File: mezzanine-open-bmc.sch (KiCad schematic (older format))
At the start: 2 parts, among them P1 CONN_02X20, P2 CONN_02X20

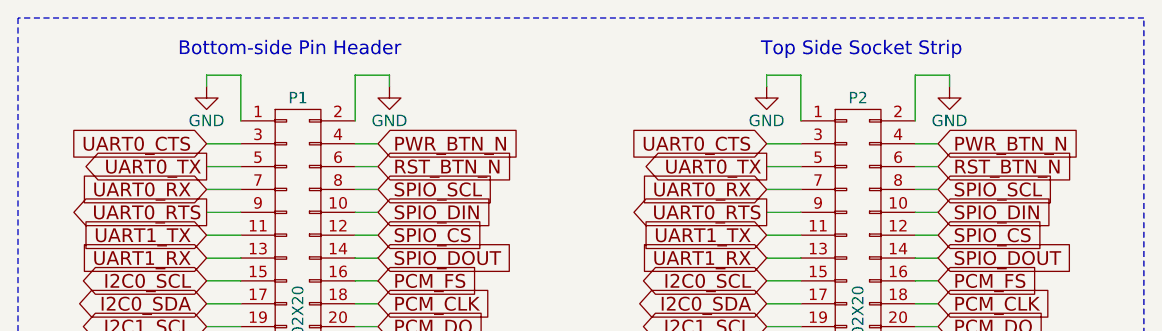
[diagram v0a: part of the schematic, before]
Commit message: Reset Project
The previous commits were based on an outdated template.
The project has been restarted with the up to date template.

Signed-off-by: Sophie Haynes <sophie.haynes@linaro.org>
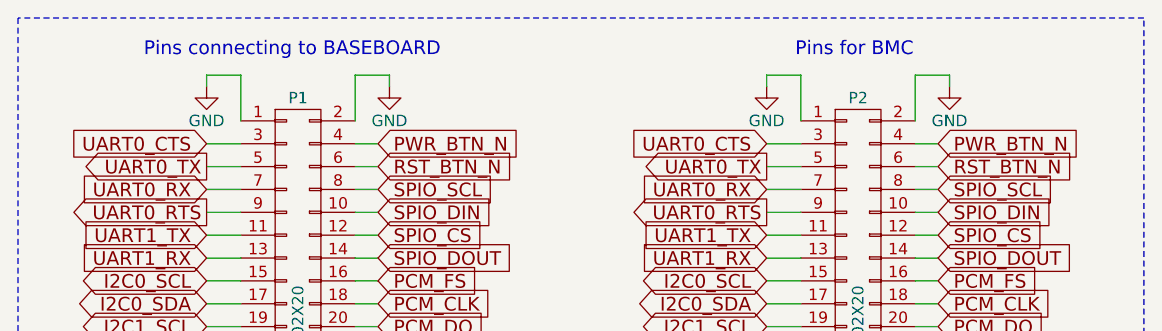
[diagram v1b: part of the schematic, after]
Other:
- note added: "Pins connecting to BASEBOARD"
- note added: "Pins for BMC"
- note removed: "Bottom-side Pin Header"
- note removed: "Top Side Socket Strip"
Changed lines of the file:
@@
 LIBS:valves
 LIBS:96boards
-LIBS:mezza-cache
+LIBS:mezzanine-open-bmc-cache
 EELAYER 25 0
 EELAYER END
@@
 Wire Wire Line
 	1650 1500 1500 1500
-Text Notes 1375 825  0    60   ~ 0
-Bottom-side Pin Header
-Text Notes 3925 825  0    60   ~ 0
-Top Side Socket Strip
+Text Notes 1225 825  0    60   ~ 0
+Pins connecting to BASEBOARD
+Text Notes 4075 825  0    60   ~ 0
+Pins for BMC
 Wire Notes Line
 	675  650  675  5475

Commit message: Change footprint for top-side socket to header
Since this board will connect to another board on top, it requires pin
connectors rather than socket connectors. These have been changed accordingly.

Signed-off-by: Sophie Haynes <sophie.haynes@linaro.org>
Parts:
- P2: footprint 96boards:Socket_Strip_SMD_2x20_Pitch2mm -> 96boards:Pin_Header_SMD_2x20_Pitch2mm
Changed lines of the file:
@@
 F 0 "P2" H 4350 3100 50  0000 C CNN
 F 1 "CONN_02X20" V 4350 2050 50  0000 C CNN
-F 2 "96boards:Socket_Strip_SMD_2x20_Pitch2mm" H 4350 1100 60  0001 C CNN
+F 2 "96boards:Pin_Header_SMD_2x20_Pitch2mm" H 4350 1100 60  0001 C CNN
 F 3 "" H 4350 1100 60  0000 C CNN
 F 4 "Yxcon" H 4350 2050 60  0001 C CNN "Mfr"
